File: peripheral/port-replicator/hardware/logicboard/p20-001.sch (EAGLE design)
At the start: 21 parts, among them IC1 74LS07N, J1 AUDIO_JACK_3.5MM_PTH, J11 DIN5, J12 DIN5, J13 DIN5, J2 AUDIO_JACK_3.5MM_PTH, J3 AUDIO_JACK_3.5MM_PTH, J4 AUDIO_JACK_3.5MM_PTH

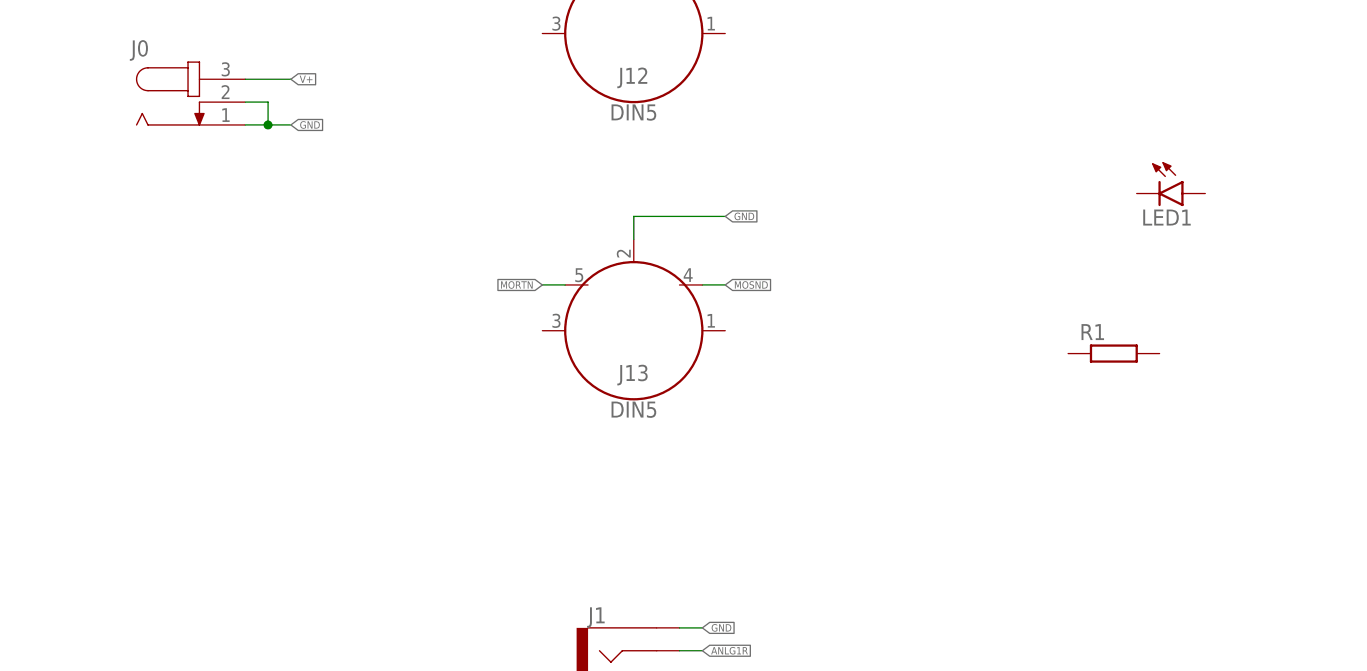
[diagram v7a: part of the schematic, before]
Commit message: Design of the port replicator.
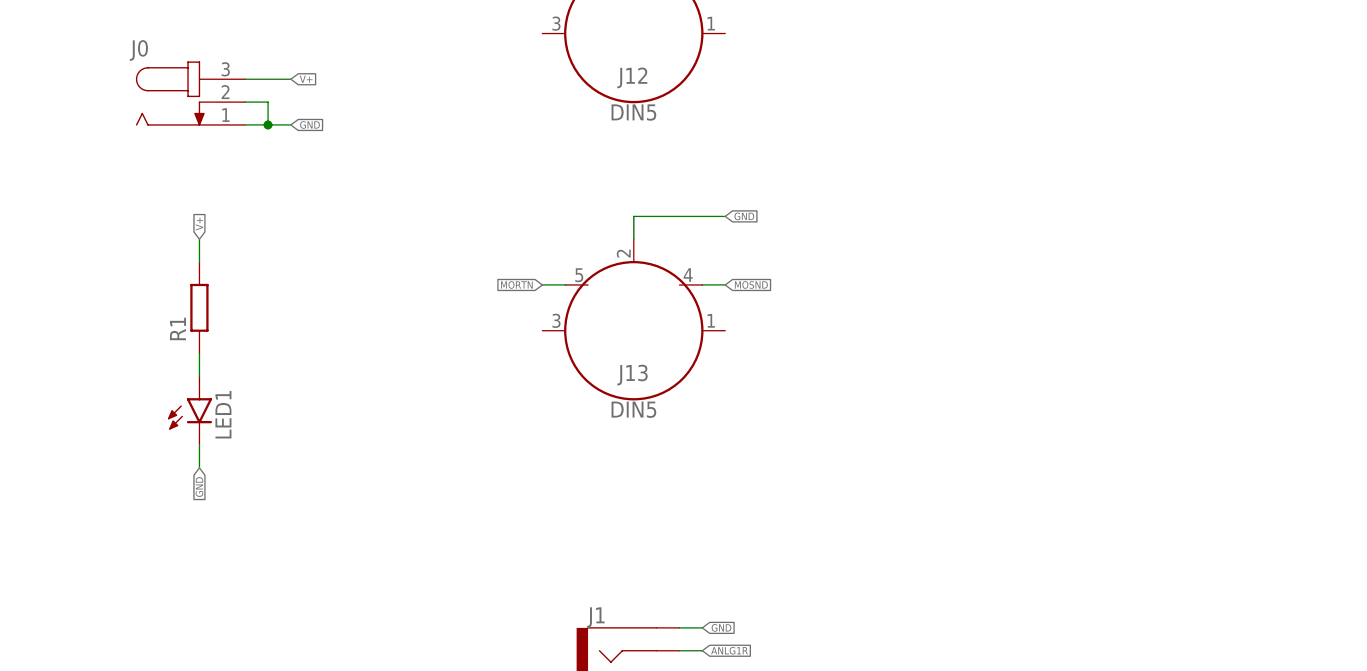
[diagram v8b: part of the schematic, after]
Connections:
- net N$3 renamed MILED
- net N$4 renamed MOLED
- new net N$4: LED1.A, R1.1
- net GND: now also LED1.C
- net V+: now also R1.2
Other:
- moved on the sheet: LED1, R1
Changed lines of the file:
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@@
 <attribute name="VALUE" x="243.84" y="66.04" size="1.778" layer="96"/>
 </instance>
-<instance part="R1" gate="G$1" x="144.78" y="170.18" smashed="yes">
-<attribute name="NAME" x="140.97" y="171.6786" size="1.778" layer="95"/>
-<attribute name="VALUE" x="140.97" y="166.878" size="1.778" layer="96"/>
+<instance part="R1" gate="G$1" x="43.18" y="175.26" smashed="yes" rot="R90">
+<attribute name="NAME" x="41.6814" y="171.45" size="1.778" layer="95" rot="R90"/>
+<attribute name="VALUE" x="46.482" y="171.45" size="1.778" layer="96" rot="R90"/>
 </instance>
 <instance part="R2" gate="G$1" x="259.08" y="157.48" smashed="yes">
@@
 <attribute name="VALUE" x="255.27" y="154.178" size="1.778" layer="96"/>
 </instance>
-<instance part="LED1" gate="G$1" x="152.4" y="187.96" smashed="yes" rot="R270">
-<attribute name="NAME" x="147.828" y="184.404" size="1.778" layer="95"/>
-<attribute name="VALUE" x="147.828" y="182.245" size="1.778" layer="96"/>
+<instance part="LED1" gate="G$1" x="43.18" y="165.1" smashed="yes">
+<attribute name="NAME" x="46.736" y="160.528" size="1.778" layer="95" rot="R90"/>
+<attribute name="VALUE" x="48.895" y="160.528" size="1.778" layer="96" rot="R90"/>
 </instance>
 <instance part="LED2" gate="G$1" x="271.78" y="157.48" smashed="yes" rot="R270">
@@
 <label x="226.06" y="119.38" size="0.8128" layer="95" rot="R180" xref="yes"/>
 </segment>
+<segment>
+<pinref part="LED1" gate="G$1" pin="C"/>
+<wire x1="43.18" y1="160.02" x2="43.18" y2="157.48" width="0.1524" layer="91"/>
+<label x="43.18" y="157.48" size="0.8128" layer="95" rot="R270" xref="yes"/>
+</segment>
 </net>
 <net name="VCC" class="2">
@@
 <label x="53.34" y="200.66" size="0.8128" layer="95" xref="yes"/>
 </segment>
+<segment>
+<pinref part="R1" gate="G$1" pin="2"/>
+<wire x1="43.18" y1="182.88" x2="43.18" y2="180.34" width="0.1524" layer="91"/>
+<label x="43.18" y="182.88" size="0.8128" layer="95" rot="R90" xref="yes"/>
+</segment>
 </net>
 <net name="LED0A" class="0">
@@
 </segment>
 </net>
-<net name="N$3" class="0">
+<net name="MILED" class="0">
 <segment>
 <pinref part="LED2" gate="G$1" pin="C"/>
@@
 </segment>
 </net>
-<net name="N$4" class="0">
+<net name="MOLED" class="0">
 <segment>
 <pinref part="LED3" gate="G$1" pin="C"/>
@@
 </segment>
 </net>
+<net name="N$4" class="0">
+<segment>
+<pinref part="R1" gate="G$1" pin="1"/>
+<pinref part="LED1" gate="G$1" pin="A"/>
+<wire x1="43.18" y1="170.18" x2="43.18" y2="167.64" width="0.1524" layer="91"/>
+</segment>
+</net>
